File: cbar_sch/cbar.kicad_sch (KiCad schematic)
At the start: 24 parts, among them J1 USB_C_Receptacle_PowerOnly_12V, SW1_PWR SW_SPST, SW2_TILT_TRIGGER SW_Push_Shielded, SW3_BATT_IND SW_Push, SW3_TILT_RESET SW_Push_Shielded, SW4_METAL SW_Push, SW5_MEAT SW_Push

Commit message: Updated schematics
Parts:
- R2: value 100 ohm -> 980 ohm
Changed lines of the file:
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@@
 			)
 		)
-		(property "Value" "100 ohm"
+		(property "Value" "980 ohm"
 			(at 158.75 110.49 90)
 			(effects

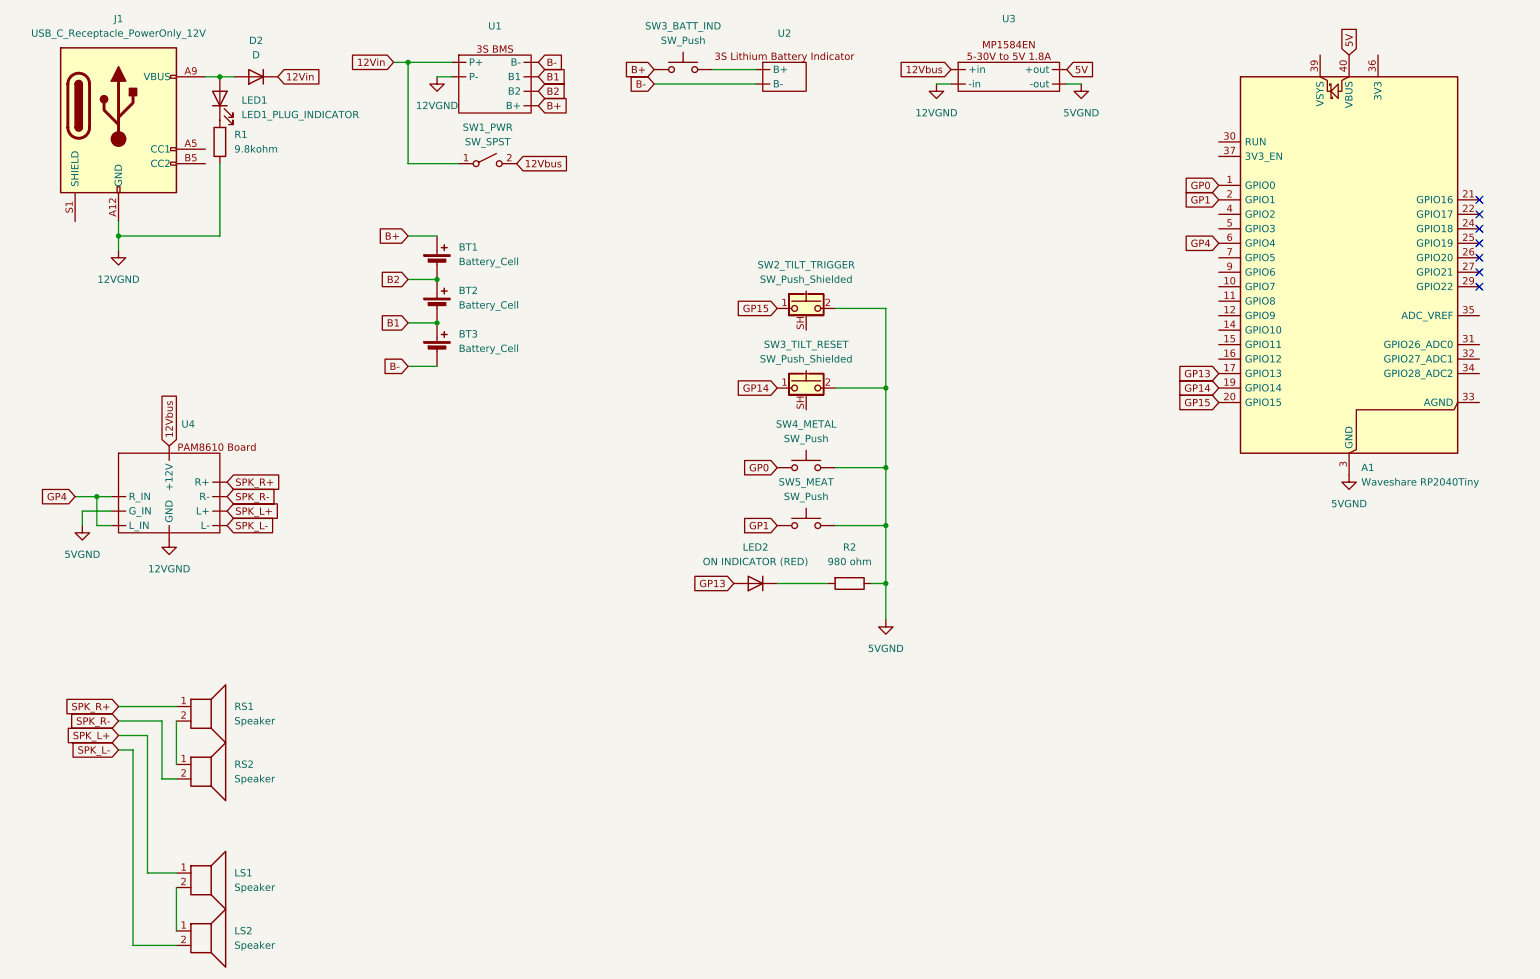
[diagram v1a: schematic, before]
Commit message: Schematic and model updates
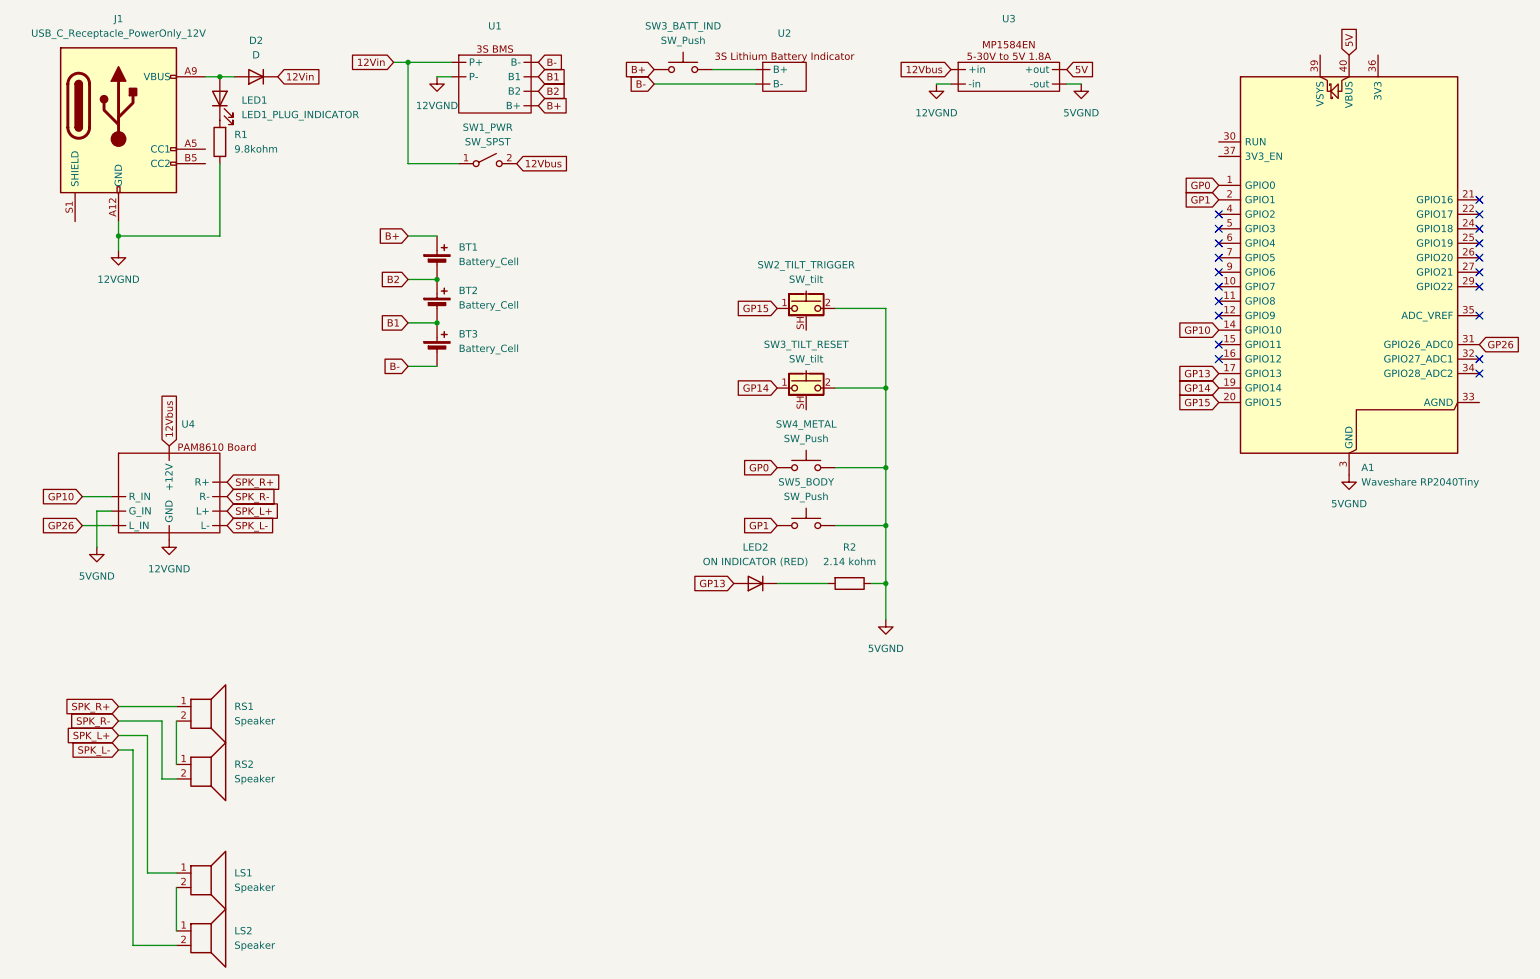
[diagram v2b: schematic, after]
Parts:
- R2: value 980 ohm -> 2.14 kohm
- SW2_TILT_TRIGGER, SW3_TILT_RESET: value SW_Push_Shielded -> SW_tilt
- renumbered SW5_MEAT to SW5_BODY
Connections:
- net GP10: now reaches A1.14 (GPIO10)
- net GP10: now also U4. (L-)
- net GP26: now reaches A1.31 (GPIO26_ADC0)
- net GP26: now also U4. (L-)
- net GP4: no longer names the net of A1.6 (GPIO4)
- net GP4: no longer U4. (L-)
- no-connect marks 7 -> 20

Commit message: Updated sch and mdl
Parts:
- R1: value 9.8kohm -> 1 Mohm
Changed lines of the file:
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@@
 			)
 		)
-		(property "Value" "9.8kohm"
+		(property "Value" "1 Mohm"
 			(at 50.8 38.0999 0)
 			(effects

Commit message: Modeling
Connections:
- net GP13: no longer A1.17 (GPIO13)
- net GP14: no longer A1.19 (GPIO14)
- net GP15: no longer A1.20 (GPIO15)
- net GP2: now reaches A1.4 (GPIO2)
- net GP3: now reaches A1.5 (GPIO3)
- net GP4: now reaches A1.6 (GPIO4)
- no-connect marks 20 -> 0
